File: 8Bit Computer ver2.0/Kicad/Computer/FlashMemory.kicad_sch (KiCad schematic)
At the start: 60 parts, among them IC198 DS1100Z-20+, IC199 SN74AHC74DR, IC200 SN74ABT245BDWR, IC201 SN74ABT245BDWR, IC202 SN74ABT245BDWR, IC203 SN74ABT245BDWR, IC204 SN74ABT245BDWR, IC205 M29F800FT55N3E2, IC206 SN74ABT245BDWR, IC207 M29F800FT55N3E2, IC208 SN74ABT245BDWR, IC209 SN74ABT245BDWR, IC210 SN74ABT245BDWR, IC211 SN74ABT245BDWR, IC212 SN74ABT245BDWR, IC213 SN74ABT245BDWR, IC214 SN74ABT245BDWR, IC215 SN74ABT245BDWR, J35 Conn_02x25_Odd_Even, J36 Conn_02x25_Odd_Even

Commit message: Fixed some Design bugs
added some pdfs
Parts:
- removed R21, R22, R24, R25, R27, R28, R29, R30: 4.7k, Resistor_SMD:R_1206_3216Metric_Pad1.30x1.75mm_HandSolder, symbol Device:R
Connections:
- net GND: now also R26.2; no longer R26.1
- net ProgModeADR: now also R26.1; no longer R26.2
- net H2ADR15: now reaches IC211.11 (B8), IC215.9 (A8)
- net H2ADR14: now reaches IC211.12 (B7), IC215.8 (A7)
- net H2ADR13: now reaches IC211.13 (B6), IC215.7 (A6)
- net H2ADR12: now reaches IC211.14 (B5), IC215.6 (A5)
- net H2ADR11: now reaches IC211.15 (B4), IC215.5 (A4)
- net H2ADR10: now reaches IC211.16 (B3), IC215.4 (A3)
- net H2ADR9: now reaches IC211.17 (B2), IC215.3 (A2)
- net H2ADR8: now reaches IC211.18 (B1), IC215.2 (A1)
- net H2ADR0: now reaches IC210.18 (B1), IC214.2 (A1)
- net H2ADR1: now reaches IC210.17 (B2), IC214.3 (A2)
- net H2ADR2: now reaches IC210.16 (B3), IC214.4 (A3)
- net H2ADR3: now reaches IC210.15 (B4), IC214.5 (A4)
- net H2ADR4: now reaches IC210.14 (B5), IC214.6 (A5)
- net H2ADR5: now reaches IC210.13 (B6), IC214.7 (A6)
- net H2ADR6: now reaches IC210.12 (B7), IC214.8 (A7)
- net H2ADR7: now reaches IC210.11 (B8), IC214.9 (A8)
- net DATd: now reaches IC199.5 (1Q), IC212.19 (~{OE})
- no-connect marks 30 -> 31
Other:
- note added: "ADR Flash Program port"
- note added: "DATA and CMD Flash Program port"
- note removed: "ADR Flash Programport"
- note removed: "DATA and CMD Flash Programport"
- moved on the sheet: C217, C218, C219, C220, C221, C222, C223, C224, C225, C226, C227, C228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

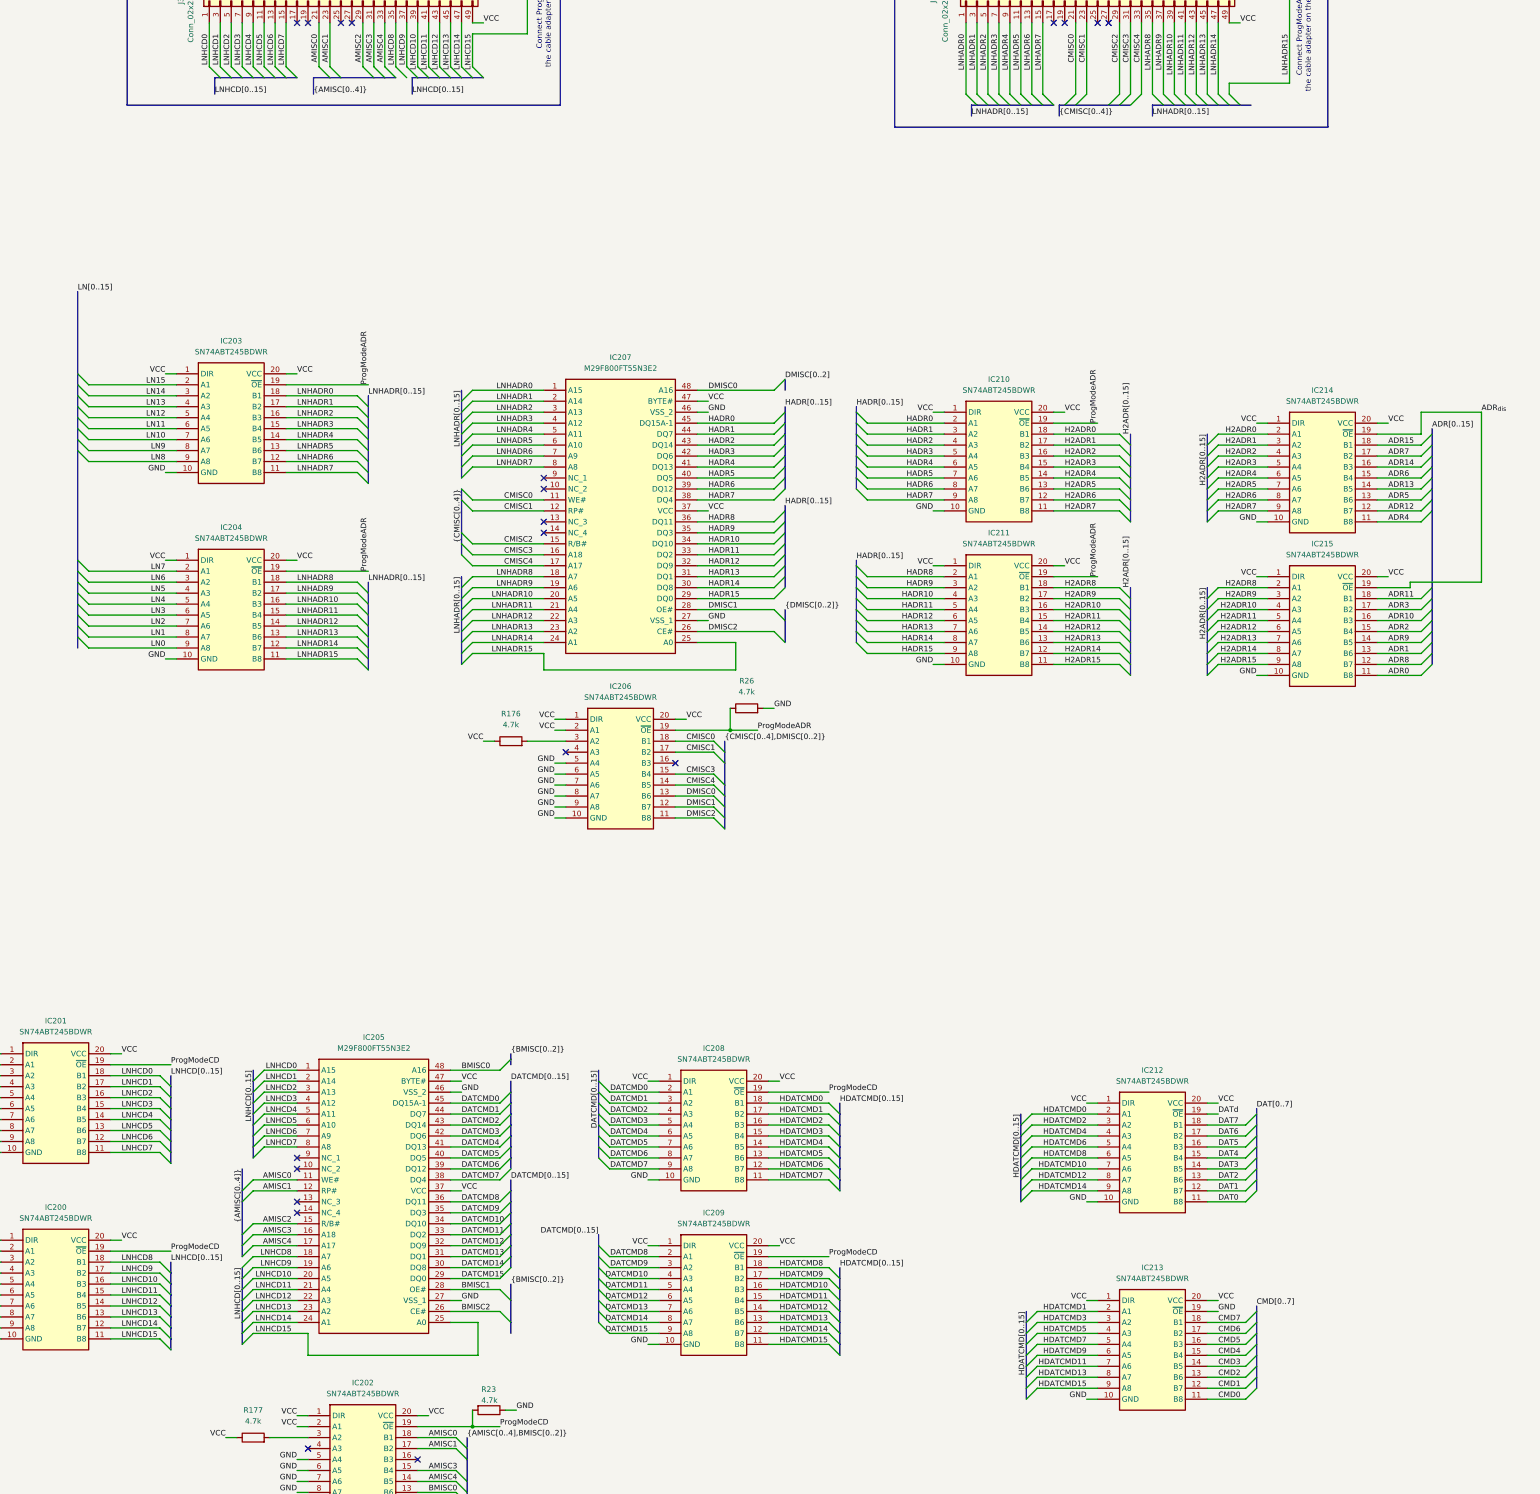
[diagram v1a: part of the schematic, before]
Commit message: part 1 of changing to A4
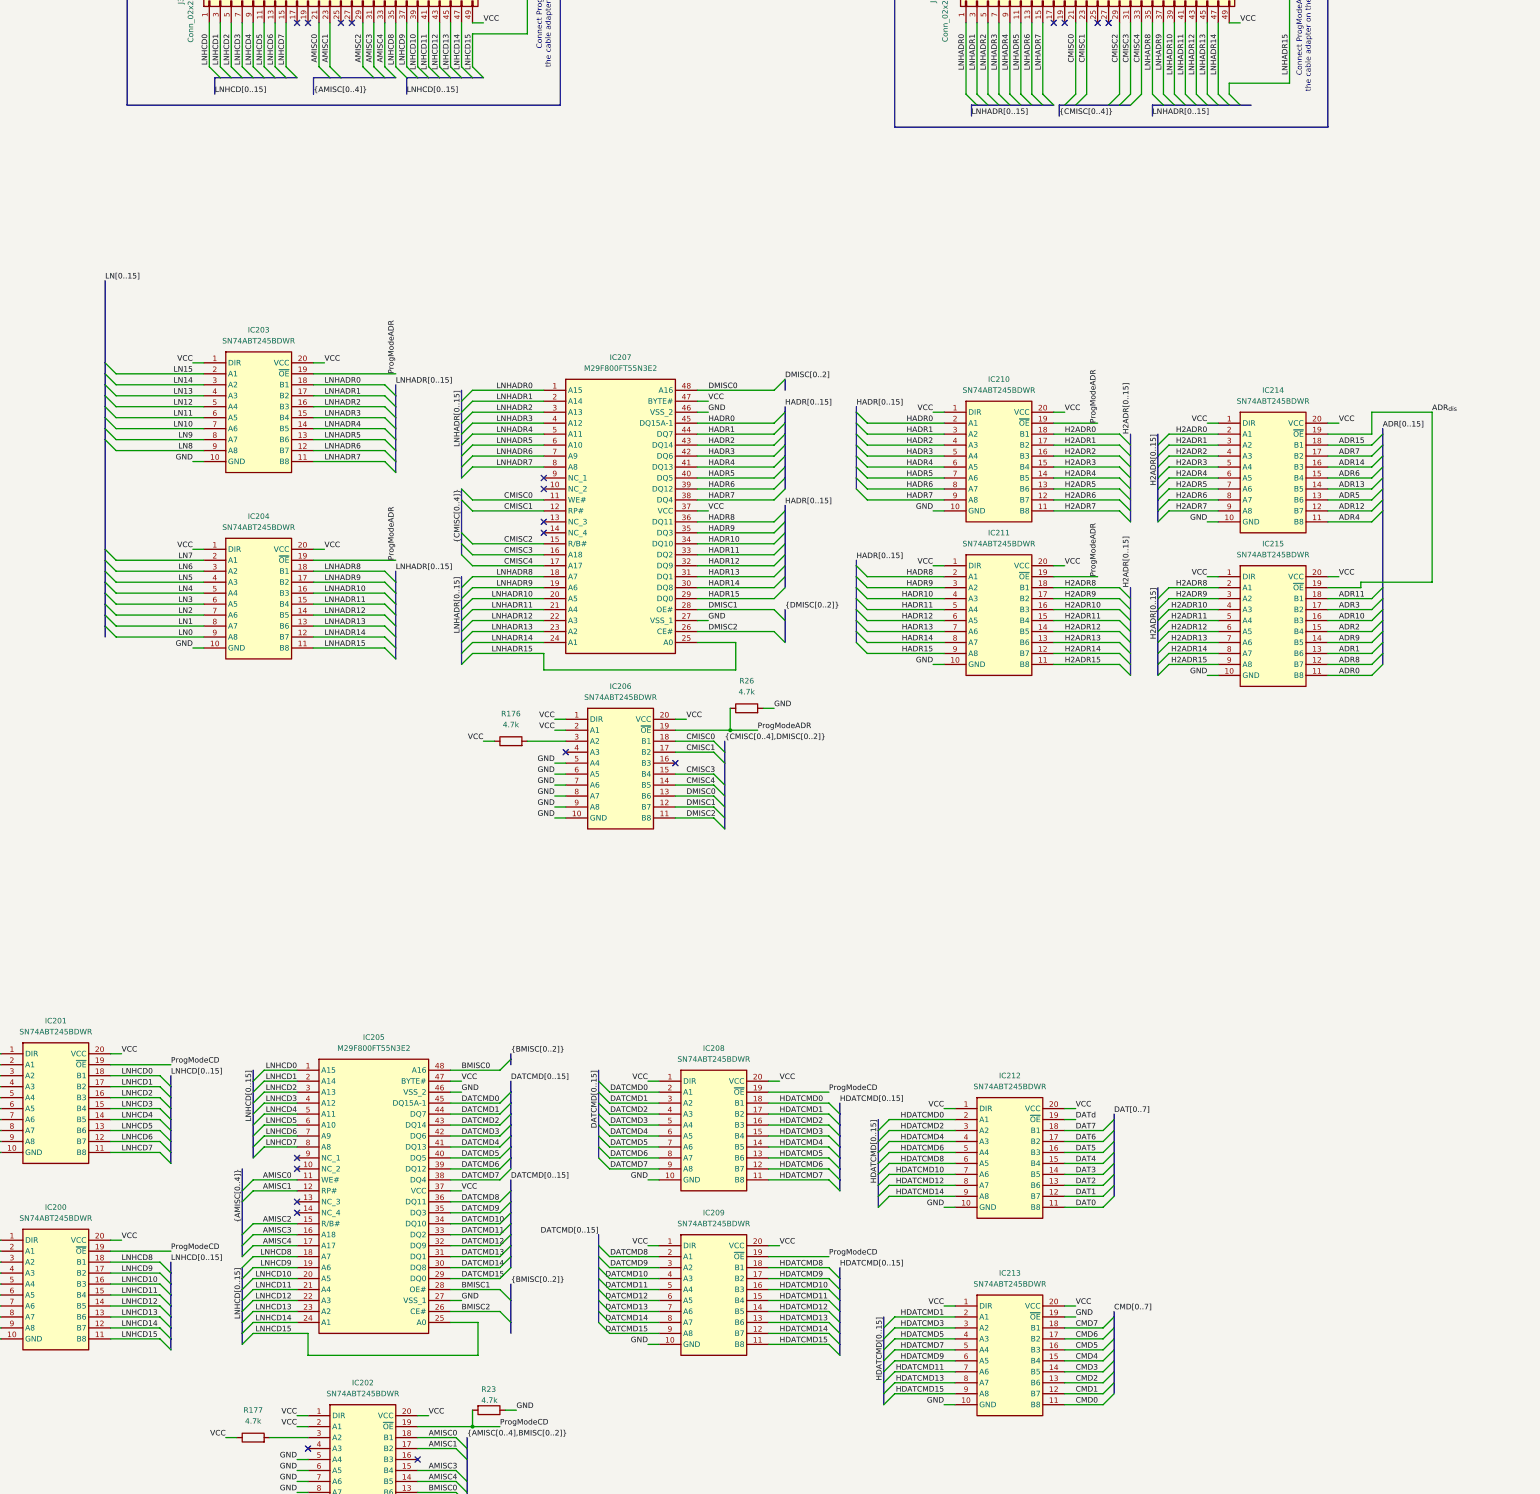
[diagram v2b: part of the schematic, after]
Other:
- moved on the sheet: IC203, IC204, IC212, IC213, IC214, IC215

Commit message: changed page numbers, compressed ROOT file from A1 to A4
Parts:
- removed IC198: DS1100Z-20+, Samacsys:SOIC127P600X175-8N, symbol Samacsys:DS1100Z-20+
- removed IC199: SN74AHC74DR, Samacsys:SOIC127P600X175-14N, symbol Samacsys:SN74AHC74DR
- removed IC200, IC201, IC202, IC203, IC204, IC206, IC208, IC209, IC210, IC211, IC212, IC213, IC214, IC215: SN74ABT245BDWR, Samacsys:SOIC127P1030X265-20N, symbol Samacsys:SN74ABT245BDWR
- removed IC205, IC207: M29F800FT55N3E2, Samacsys:SOP50P2000X120-48N, symbol Samacsys:M29F800FT55N3E2
- removed J35, J36: Conn_02x25_Odd_Even, Connector_PinHeader_2.54mm:PinHeader_2x25_P2.54mm_Vertical, symbol Connector_Generic:Conn_02x25_Odd_Even
- removed R176, R177, R23, R26: 4.7k, Resistor_SMD:R_1206_3216Metric_Pad1.30x1.75mm_HandSolder, symbol Device:R
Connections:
- no-connect marks 31 -> 0
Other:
- added sheet ADR_Flash (ADR_Flash.kicad_sch)
- added sheet CMD_DAT_Flash (CMD_DAT_Flash.kicad_sch)
- note removed: "ADR Flash Program port"
- note removed: "Connect ProgModeADR to VCC via the cable adapter on the programmer side"
- note removed: "Connect ProgModeCD to VCC via the cable adapter on the programmer side"
- note removed: "DATA and CMD Flash Program port"
- moved on the sheet: C217, C218, C219, C220, C221, C222, C223, C224, C225, C226, C227, C228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

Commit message: changed page numbers, every schematic is now A4
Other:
- title: (none) -> ${SHEETNAME}
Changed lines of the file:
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@@
 	(generator_version "9.0")
 	(paper "A4")
+	(title_block
+		(title "${SHEETNAME}")
+		(date "2026-03-21")
+		(rev "2.7")
+	)
 	(junction
 		(at 123.19 161.29)
@@
 			(project "Computer"
 				(path "/1196a00e-6878-4d6d-82b7-9e052dfe7c14/13a36bad-d32b-469d-8a9a-941e54d6dd87/af9afd94-c55f-4e9c-afa1-53e0d366f8d9"
-					(page "24")
+					(page "46")
 				)
 			)
@@
 			(project "Computer"
 				(path "/1196a00e-6878-4d6d-82b7-9e052dfe7c14/13a36bad-d32b-469d-8a9a-941e54d6dd87/af9afd94-c55f-4e9c-afa1-53e0d366f8d9"
-					(page "25")
+					(page "47")
 				)
 			)
